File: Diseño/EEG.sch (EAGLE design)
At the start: 19 parts, among them IC1 REF2033AIDDCT

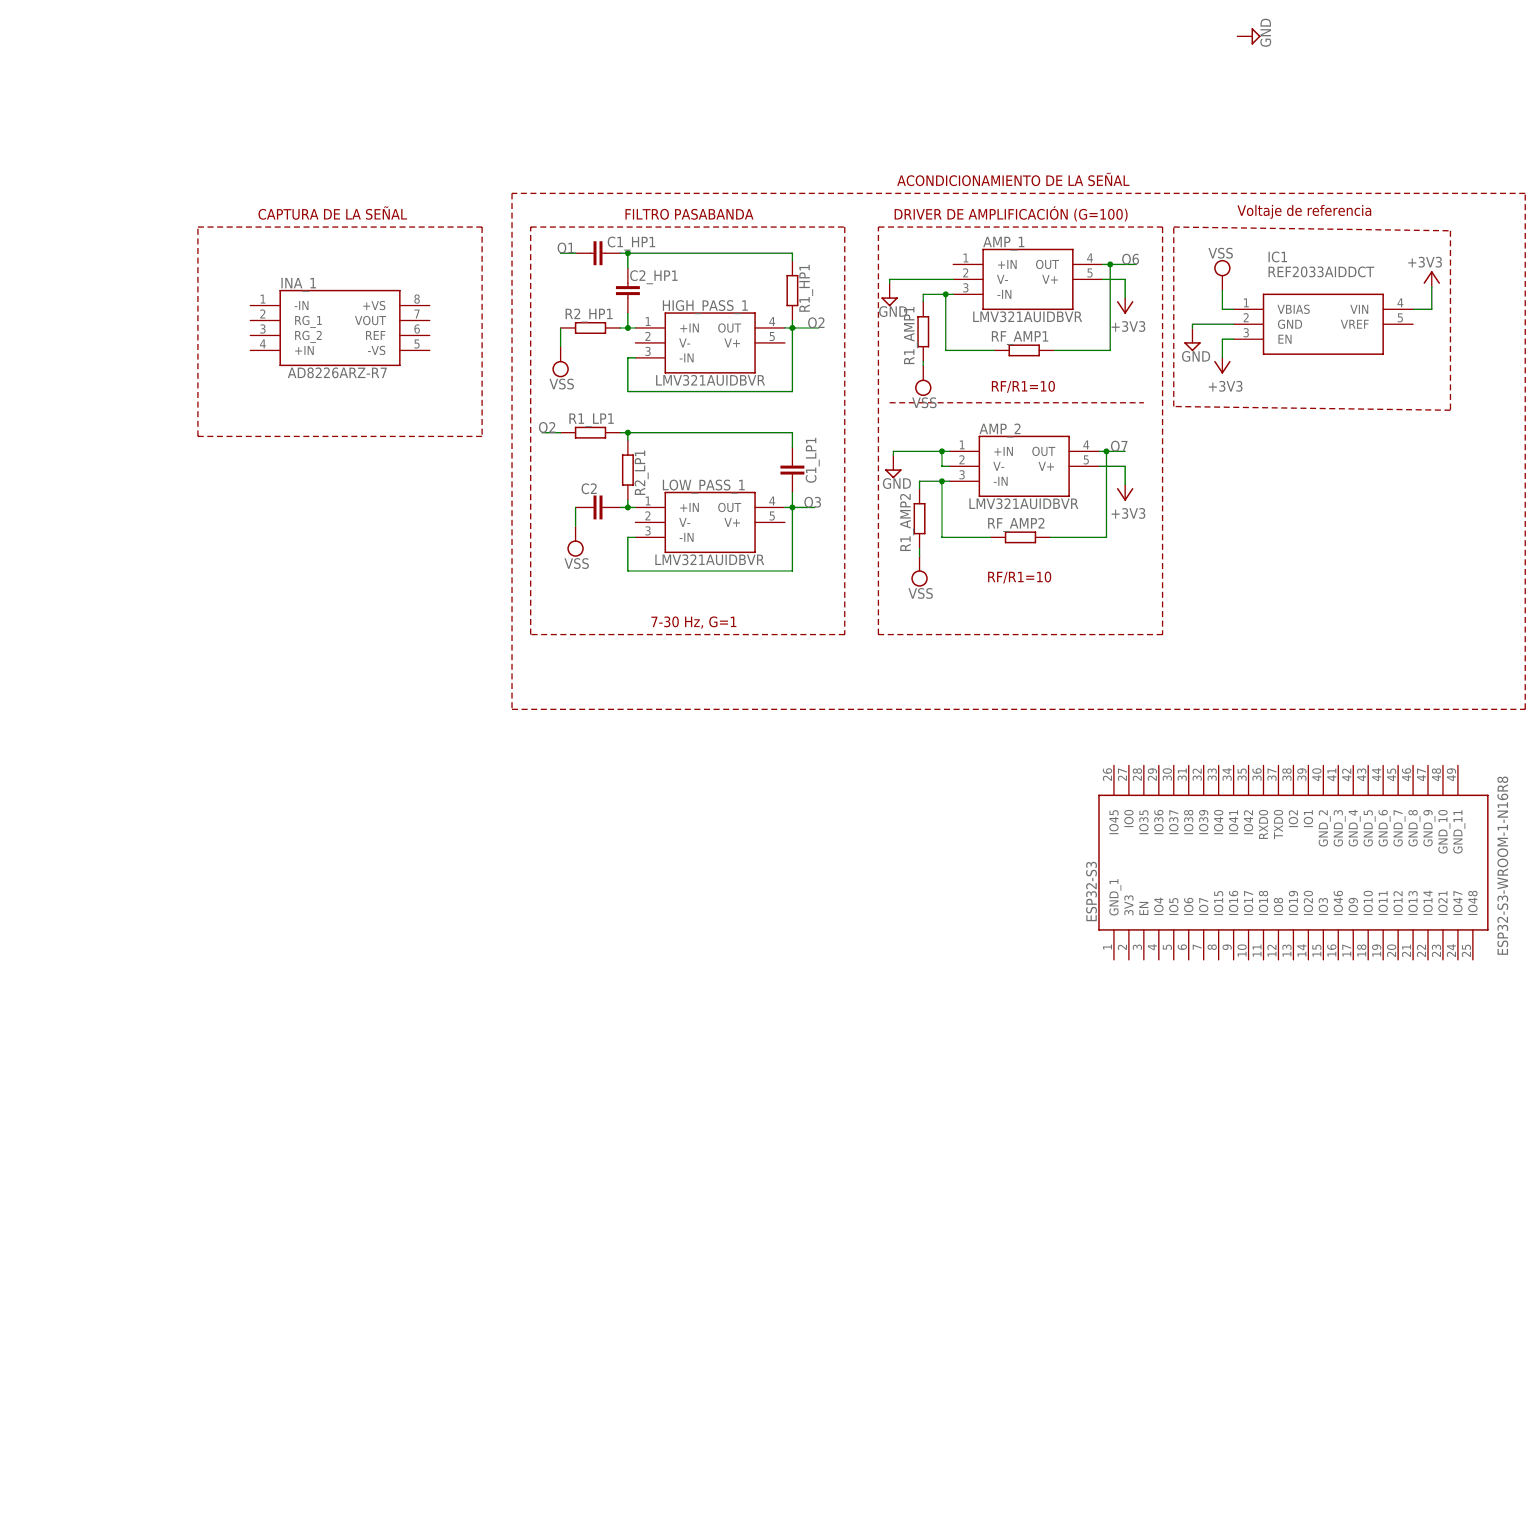
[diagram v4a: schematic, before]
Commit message: Añadido circuito de carga v3
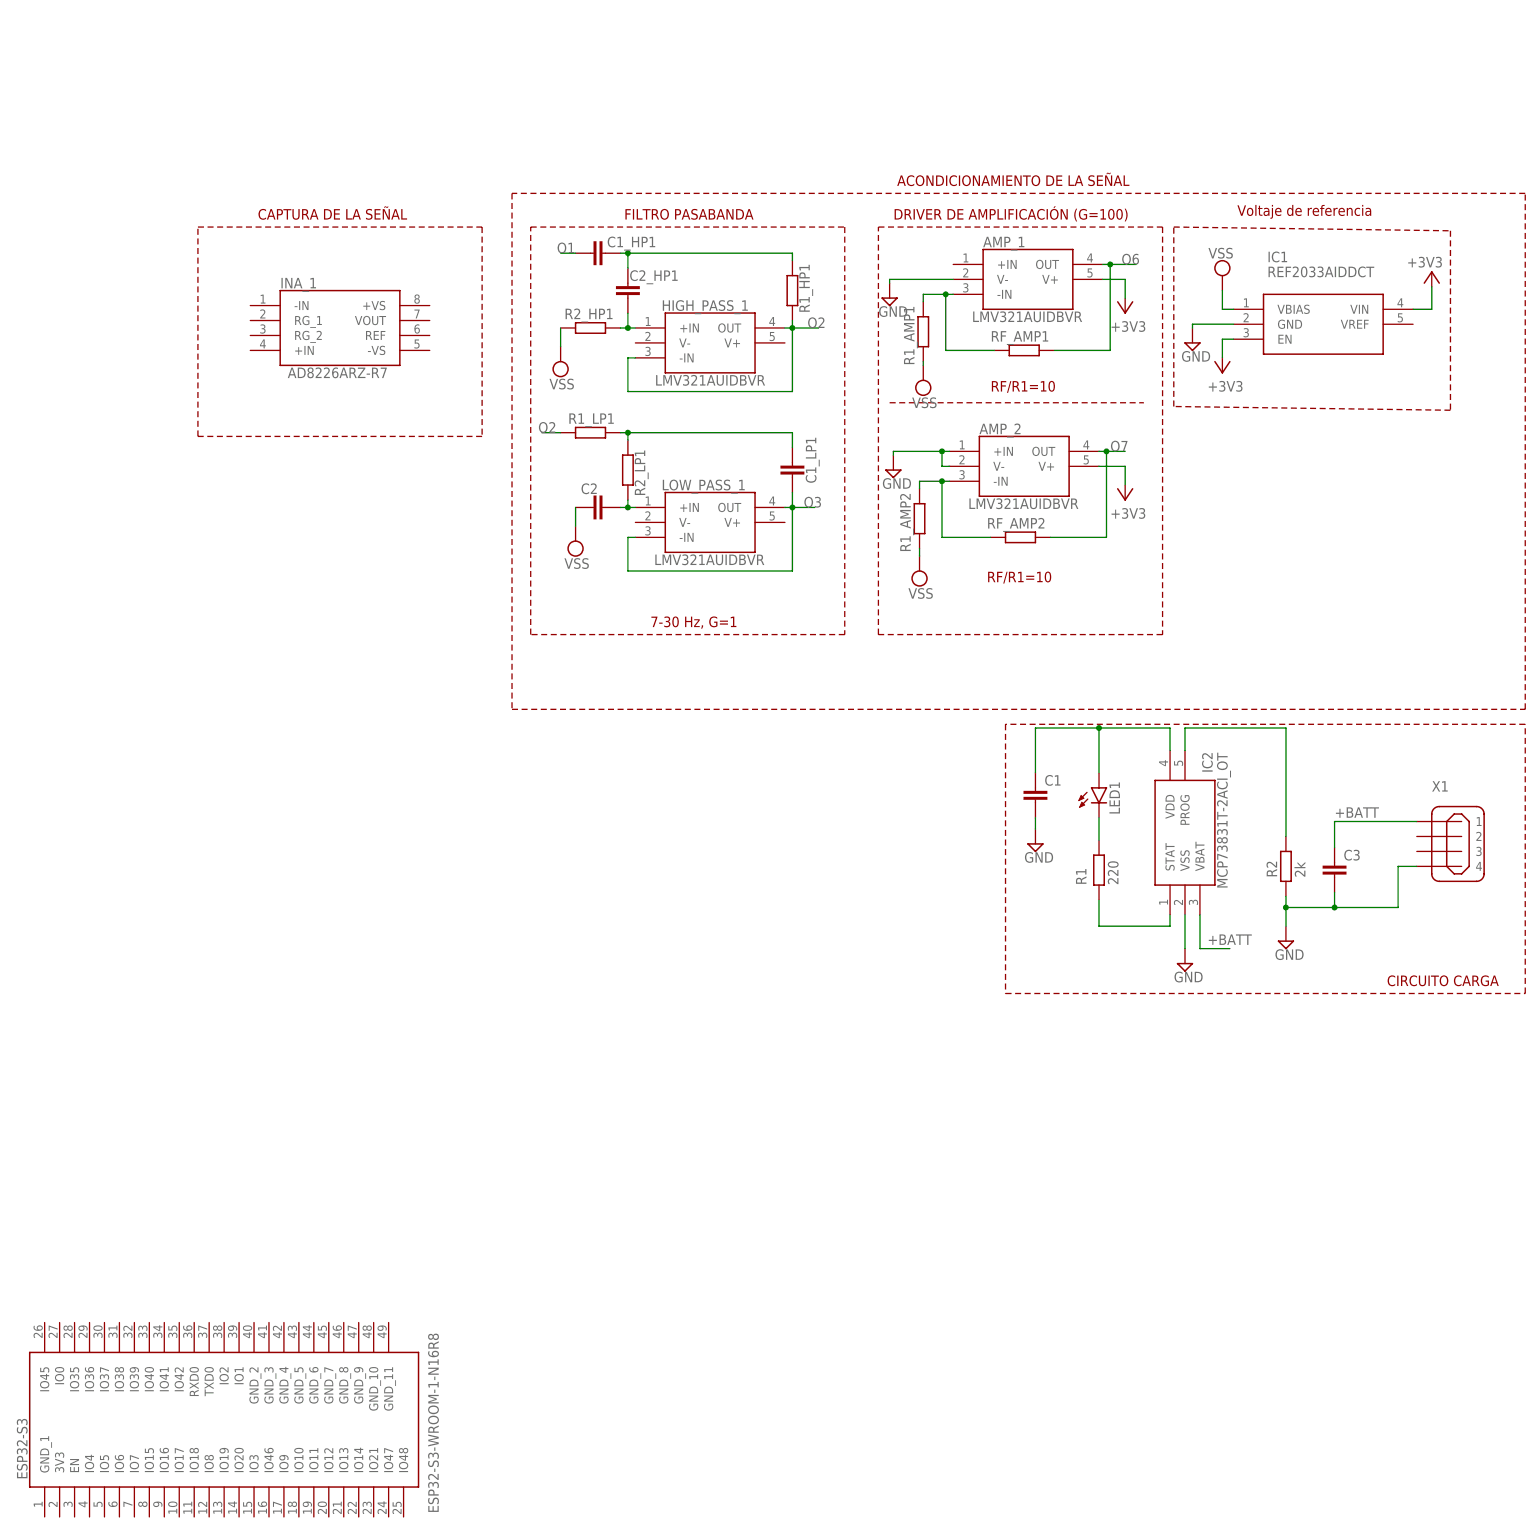
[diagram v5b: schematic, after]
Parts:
- added C1, C3: (no value), rcl:C-EUC0805K
- added IC2: MCP73831T-2ACI_OT, MCP73831T-2ACI_OT:MCP73831T-2ACI_OT
- added LED1: (no value), led:LEDCHIPLED_0805
- added R1: 220, rcl:R-EU_R0805
- added R2: 2k, rcl:R-EU_R0805
- added X1: MINI-USB_4P-85-32004-40X, con-cypressindustries:MINI-USB_4P-85-32004-40X
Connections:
- new net +BATT: C3.1, IC2.VBAT, X1.1
- new net N$1: C1.1, IC2.VDD, LED1.A
- new net N$10: IC2.STAT, R1.1
- new net N$2: IC2.PROG, R2.2
- new net N$3: LED1.C, R1.2
- net GND: now also C1.2, C3.2, IC2.VSS, R2.1, X1.4
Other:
- note added: "CIRCUITO CARGA"
- moved on the sheet: ESP32-S3

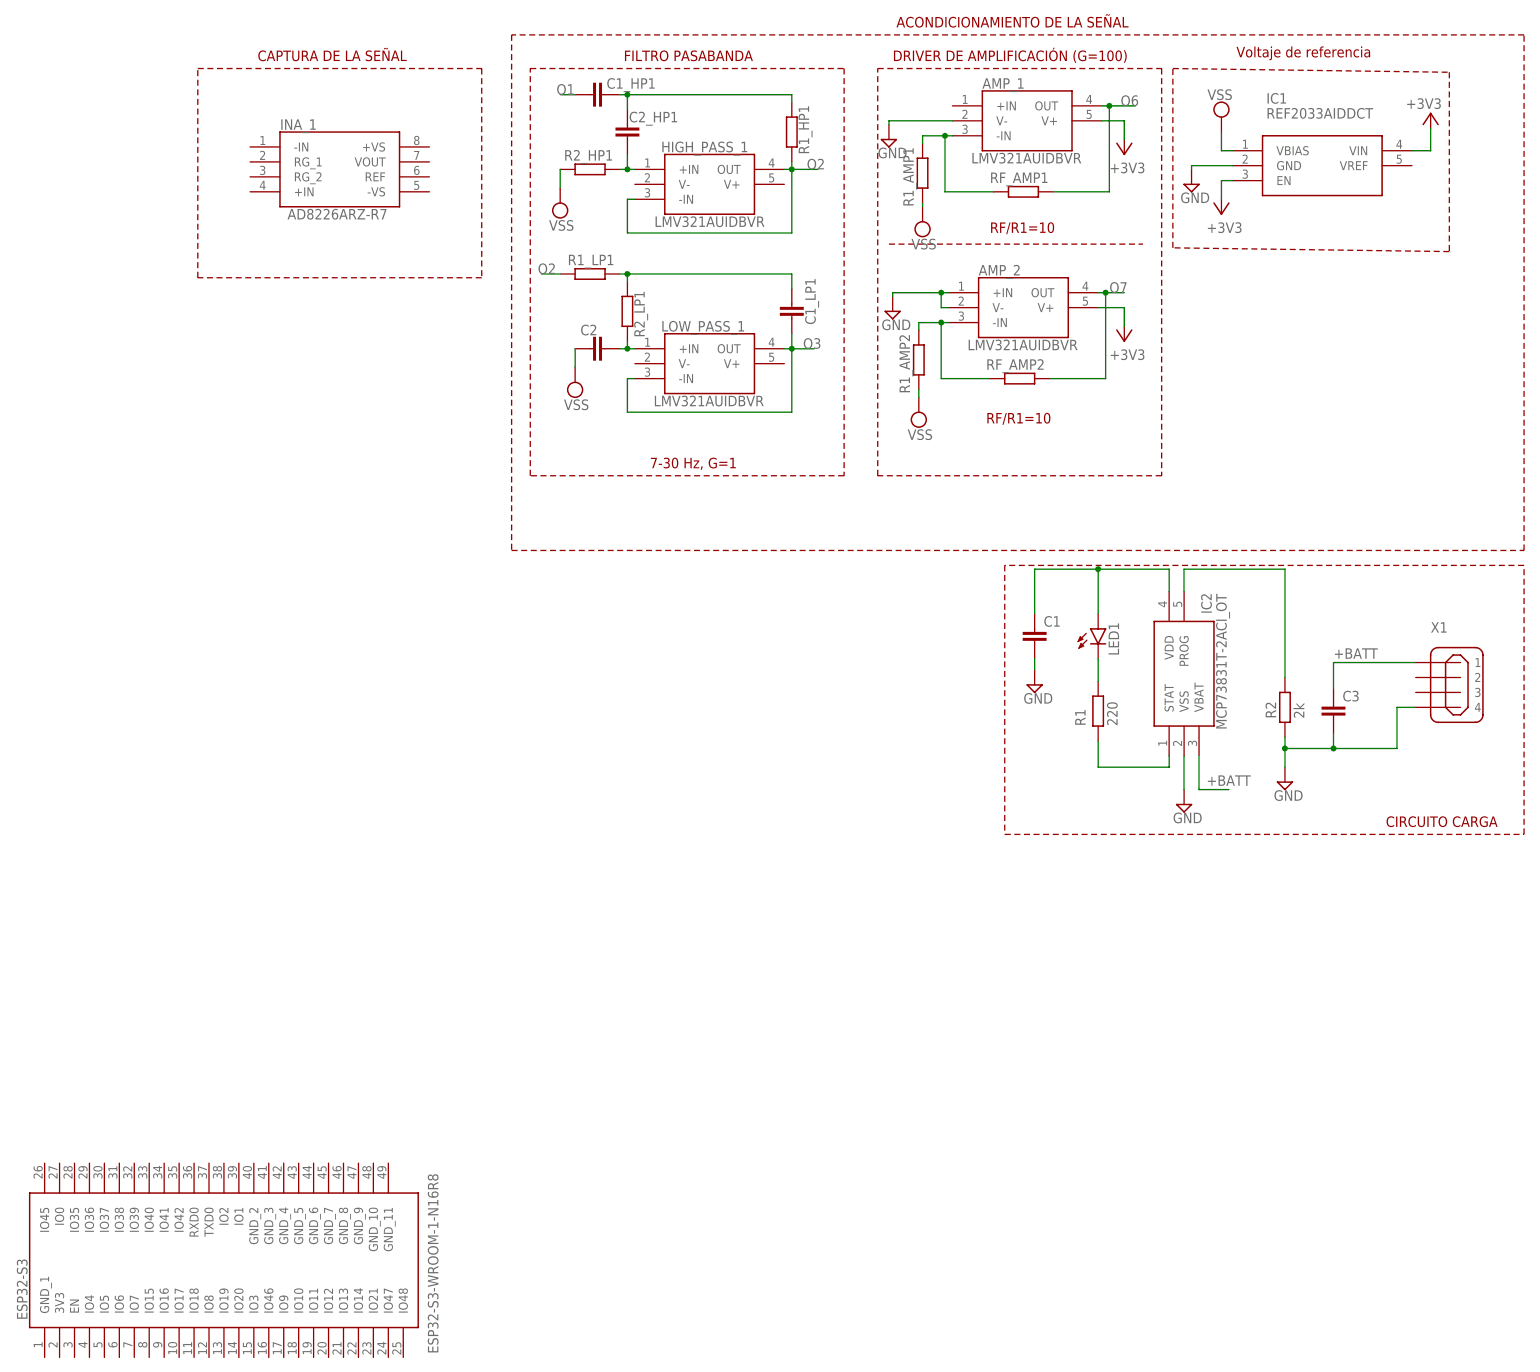
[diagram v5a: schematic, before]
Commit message: Añadí el regulador de 3V3 (Low Dropout)
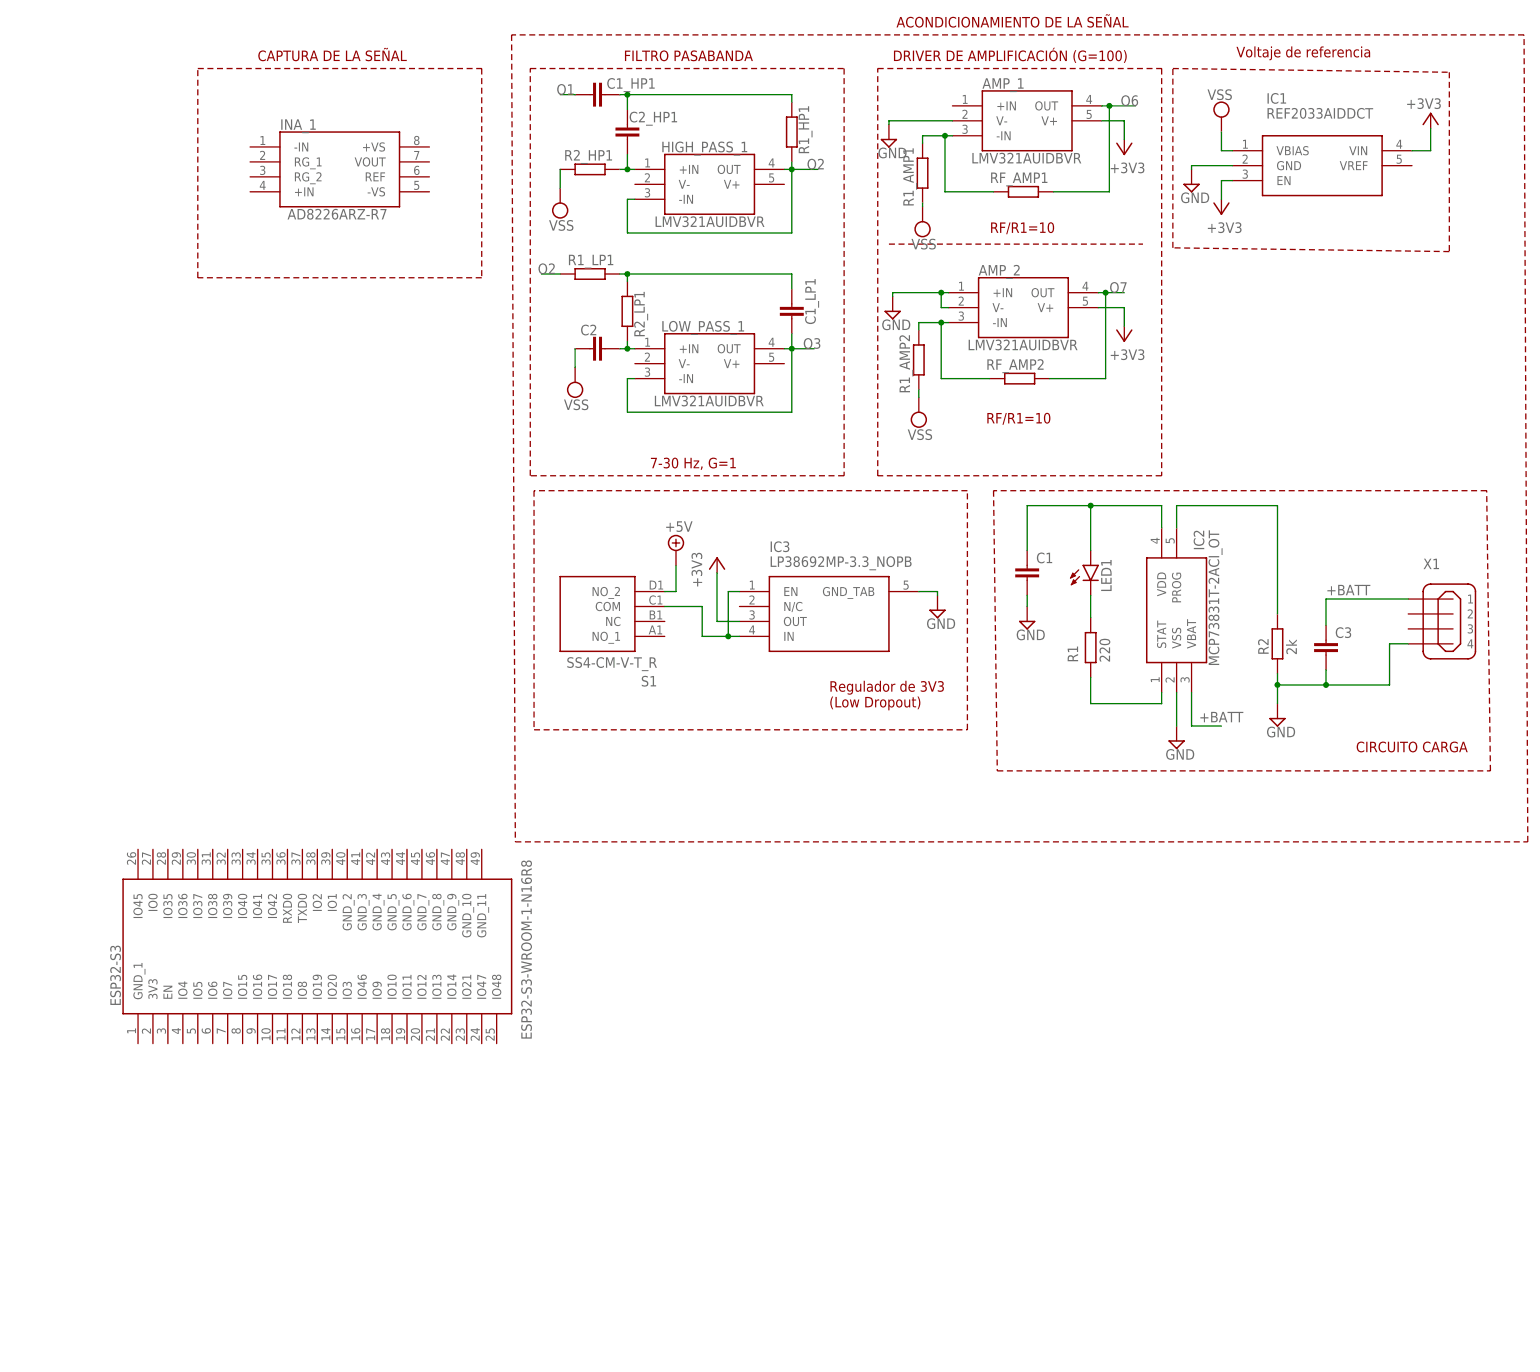
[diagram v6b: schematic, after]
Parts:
- added IC3: LP38692MP-3.3_NOPB, LP38692MP-3.3_NOPB:LP38692MP-3.3_NOPB
- added S1: SS4-CM-V-T_R, SS4-CM-V-T_R:SS4-CM-V-T_R
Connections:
- new net +5V: S1.NO_2
- new net N$11: IC3.EN, IC3.IN, S1.COM
- net +3V3: now also IC3.OUT
- net GND: now also IC3.GND_TAB
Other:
- note added: "Regulador de 3V3 (Low Dropout)"
- moved on the sheet: C1, C3, ESP32-S3, IC2, LED1, R1, R2, X1
